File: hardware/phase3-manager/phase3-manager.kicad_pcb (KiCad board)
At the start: 2 copper layers, 100 x 80 mm, 87 parts, among them J1 BACKPLANE, J3 USB-C, J4 UART, J5 PANEL KEYS, J6 ILI9341 LCD MODULE, Q10 2N7002, Q11 AO3401A-class PMOS, Q8 2N7002, Q9 2N7002, SW1 RESET, SW2 BOOT, U10 ESP32-S3-WROOM-1-N8R2, U11 TCAN1042HGV, U12 TPD2E001, U13 TCA9535PWR, U8 LMR36015AQRNXRQ1, U9 NCP1117-3.3

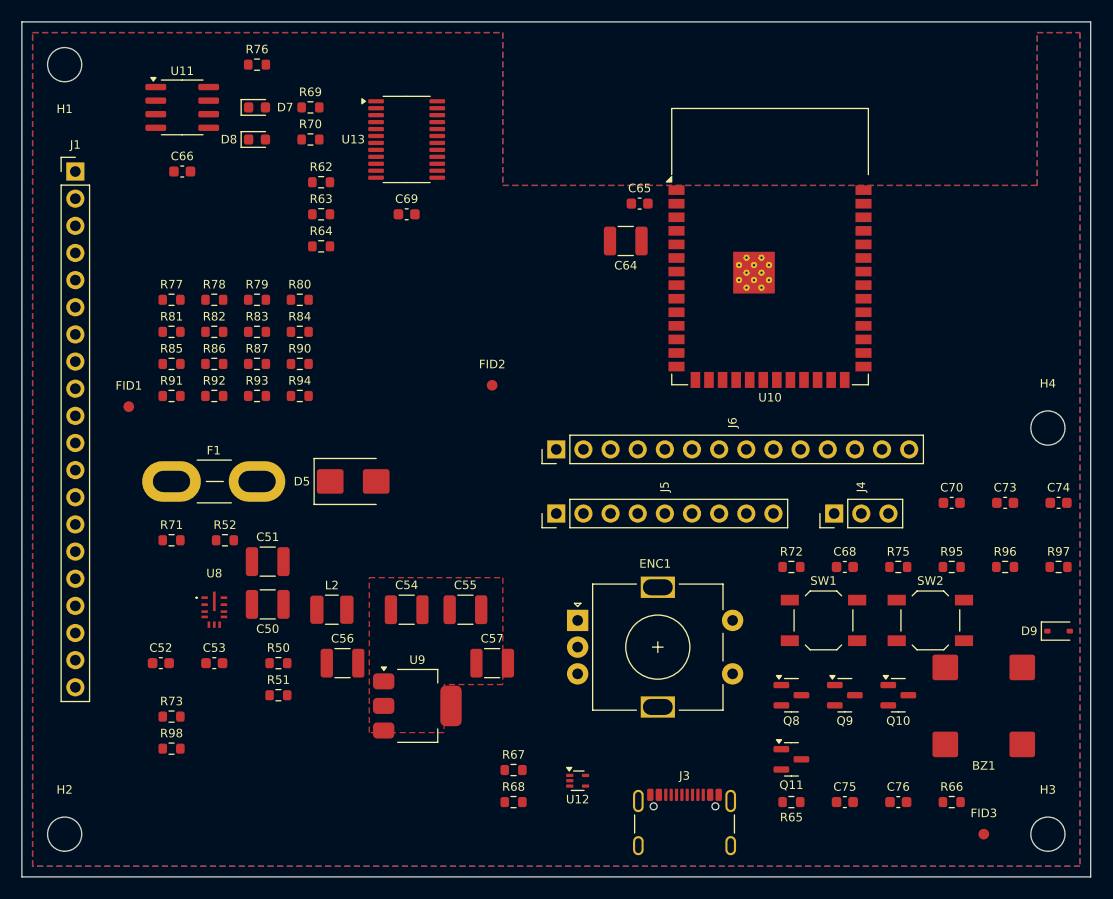
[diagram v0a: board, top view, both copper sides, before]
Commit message: Route the phase-3 manager board: 0 unconnected, 0 DRC errors
Hand-drawn locked copper for the USB pair (through U12 into J3), the CAN
pair and the U8 buck power stage (route_critical.py), then Freerouting
with B.Cu weighted expensive, phase-1's finish_routes with 2-layer
settings, and PGND stitching between the two ground pours.

PGND is now poured on both layers (3V3 runs as 0.4 mm tracks). Placement
in gen_board.py was reworked against the netlist and U8 gets an IPC-size
board-local courtyard. Fab outputs regenerated.

phase1 finish_routes.py gains FILL_AROUND/B_COST hooks (defaults keep
phase-1 behaviour), skips rule areas, and loads the base board first so
LoadBoard no longer resets the project rules.

Co-Authored-By: Claude Opus 5.5 (1M context) <noreply@anthropic.com>
Claude-Session: https://claude.ai/code/session_01KfJo5gk19gMQupM6RFmYmb
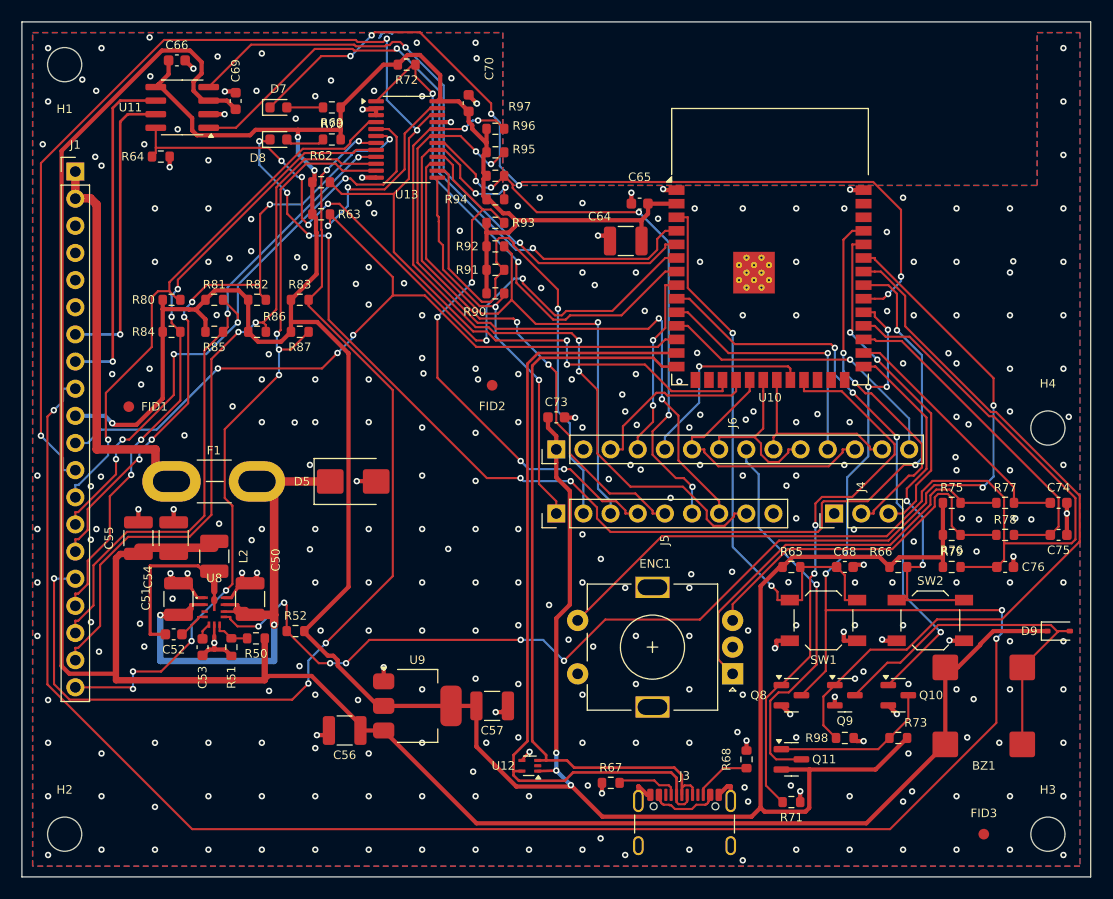
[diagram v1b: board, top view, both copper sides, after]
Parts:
- moved R77 80.3 mm to (112.0, 65.0)
- moved R76 78.5 mm to (107.0, 68.0)
- moved R78 77.2 mm to (112.0, 68.0)
- moved R79 69.6 mm to (107.0, 71.0)
- moved R73 68.0 mm to (102.0, 87.0)
- moved R97 66.8 mm to (64.3, 30.0)
- moved R98 63.0 mm to (97.0, 87.0)
- moved R71 63.0 mm to (92.0, 93.0)
- moved R96 61.5 mm to (64.3, 32.2)
- moved R72 59.2 mm to (56.0, 24.0)
- moved C70 58.7 mm to (61.8, 27.6), turned to 90 degrees
- moved R95 56.2 mm to (64.3, 34.4)
- moved C73 42.8 mm to (70.0, 57.0)
- moved R91 32.5 mm to (64.3, 43.2)
- moved C75 32.0 mm to (117.0, 68.0)
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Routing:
- net 3V3: track 0.00 -> 337.8 mm, vias 0 -> 6
- net 5V0: track 0.00 -> 209.6 mm
- net HW_EN: track 0.00 -> 196.9 mm, vias 0 -> 7
- net I2C_SCL: track 0.00 -> 137.7 mm, vias 0 -> 5
- net AUX_PG: track 0.00 -> 112.8 mm, vias 0 -> 8
- net LED_CAN: track 0.00 -> 109.9 mm, vias 0 -> 8
- net PRESENT3: track 0.00 -> 98.0 mm, vias 0 -> 5
- net ENC_SW: track 0.00 -> 93.8 mm
- net I2C_SDA: track 0.00 -> 93.5 mm, vias 0 -> 5
- net LED_STAT: track 0.00 -> 82.9 mm, vias 0 -> 6
- net USB_DN: track 0.00 -> 74.3 mm
- net PRESENT7: track 0.00 -> 73.9 mm, vias 0 -> 7
- net CAN_STB: track 0.00 -> 71.2 mm, vias 0 -> 6
- net USB_DP: track 0.00 -> 69.4 mm
- net BUZZ: track 0.00 -> 69.2 mm
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- added copper zone on F.Cu, net PGND
- removed copper zone on F.Cu, net 3V3
- removed copper zone on F.Cu, net 5V0
